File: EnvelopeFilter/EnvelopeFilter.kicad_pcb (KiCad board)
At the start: 2 copper layers, 49.5 x 97.8 mm, 58 parts, among them J1 Conn_01x02_Male, J2 Conn_01x03_Male, J3 Conn_01x03_Male, J4 Conn_01x03_Male, J5 Conn_01x03_Male, J6 Conn_01x03_Male, J7 Conn_01x03_Male, J8 Conn_01x03_Male, J9 Conn_01x09_Male, U1 AS3320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

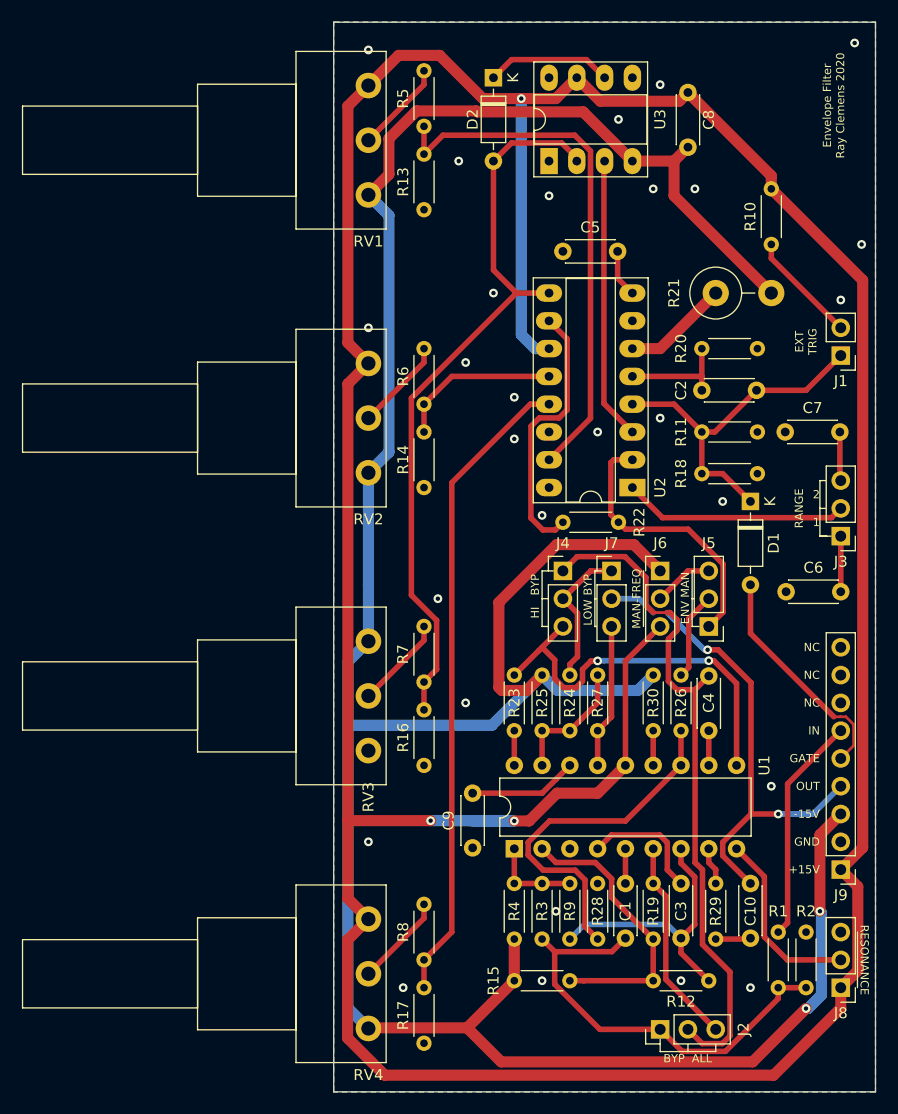
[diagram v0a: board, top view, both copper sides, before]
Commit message: Minor EnvelopeFilter changes, created SummingAmp
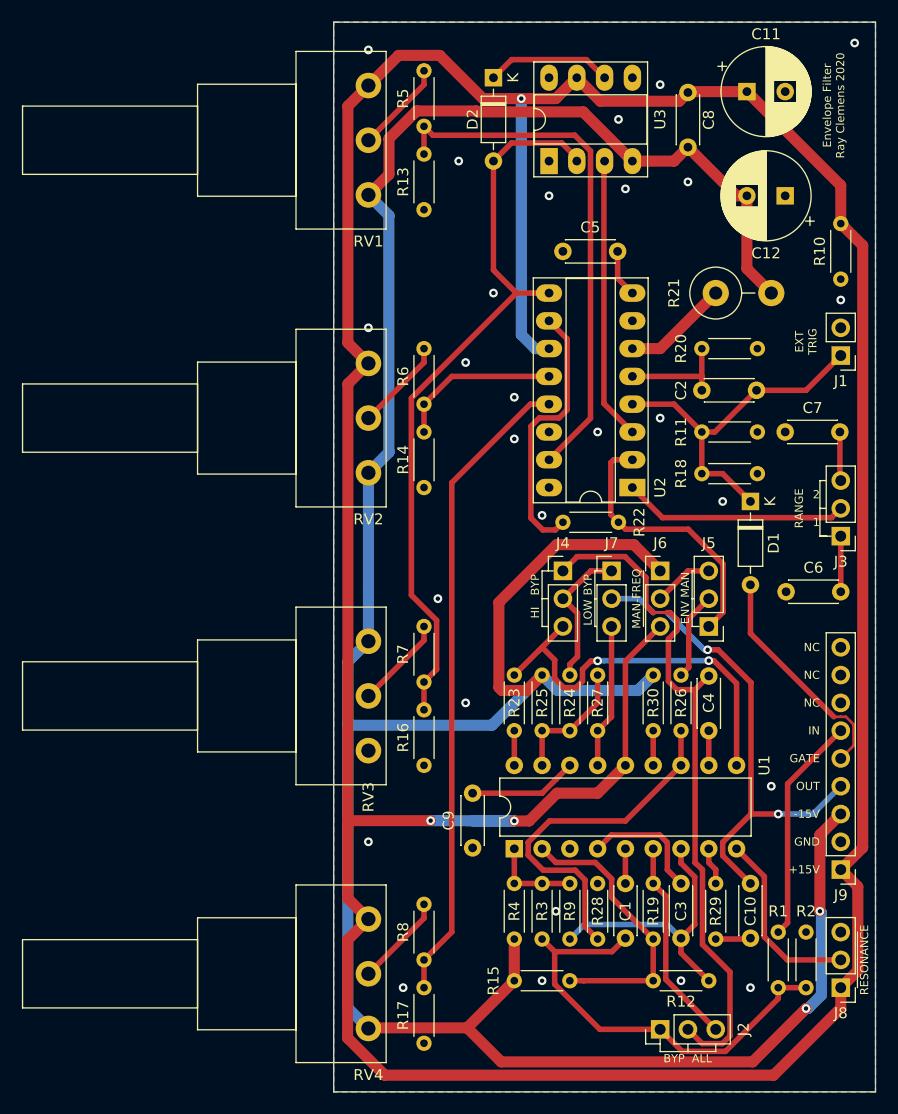
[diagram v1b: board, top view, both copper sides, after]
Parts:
- added C11: 100uF, Capacitor_THT:CP_Radial_D8.0mm_P3.50mm, F.Cu at (165.4, 53.3)
- added C12: 100uF, Capacitor_THT:CP_Radial_D8.0mm_P3.50mm, F.Cu at (168.9, 62.9)
- C1, C3, C4, C9: value 1n -> 1nF
- C10: value 1u -> 1uF
- C5, R11: value 10n -> 10nF
- C7: value 33n -> 33nF
- C8: value 0.1u -> 0.1uF
- moved R10 7.10 mm to (174.0, 70.5)
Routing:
- net Net-(J1-Pad2): track 10.3 -> 0.00 mm
- net +15V: track 336.4 -> 339.7 mm
- net -15V: track 266.4 -> 267.7 mm
- net GND: vias 28 -> 27
